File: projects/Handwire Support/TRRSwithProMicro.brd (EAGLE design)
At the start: 34.3 x 33 mm, 5 parts, among them SW1 RSTSWSMD

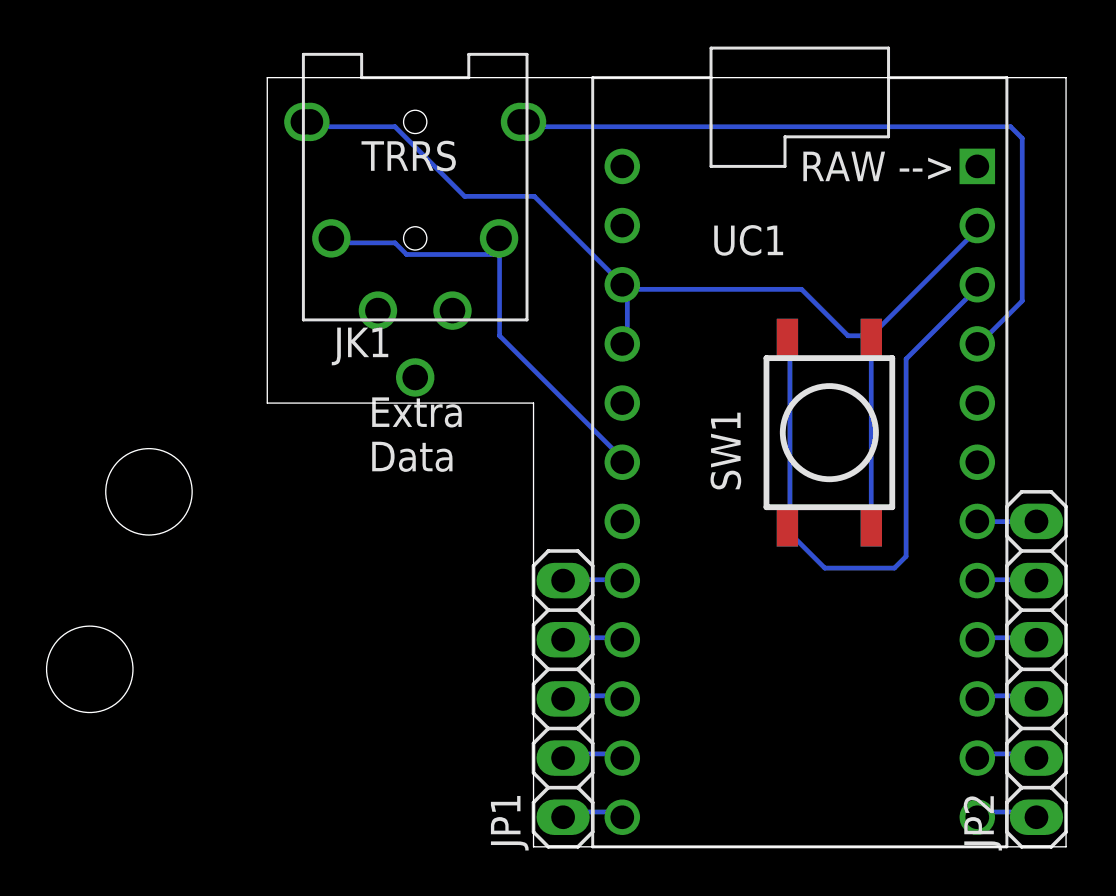
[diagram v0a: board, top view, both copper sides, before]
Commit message: Reversible handwires
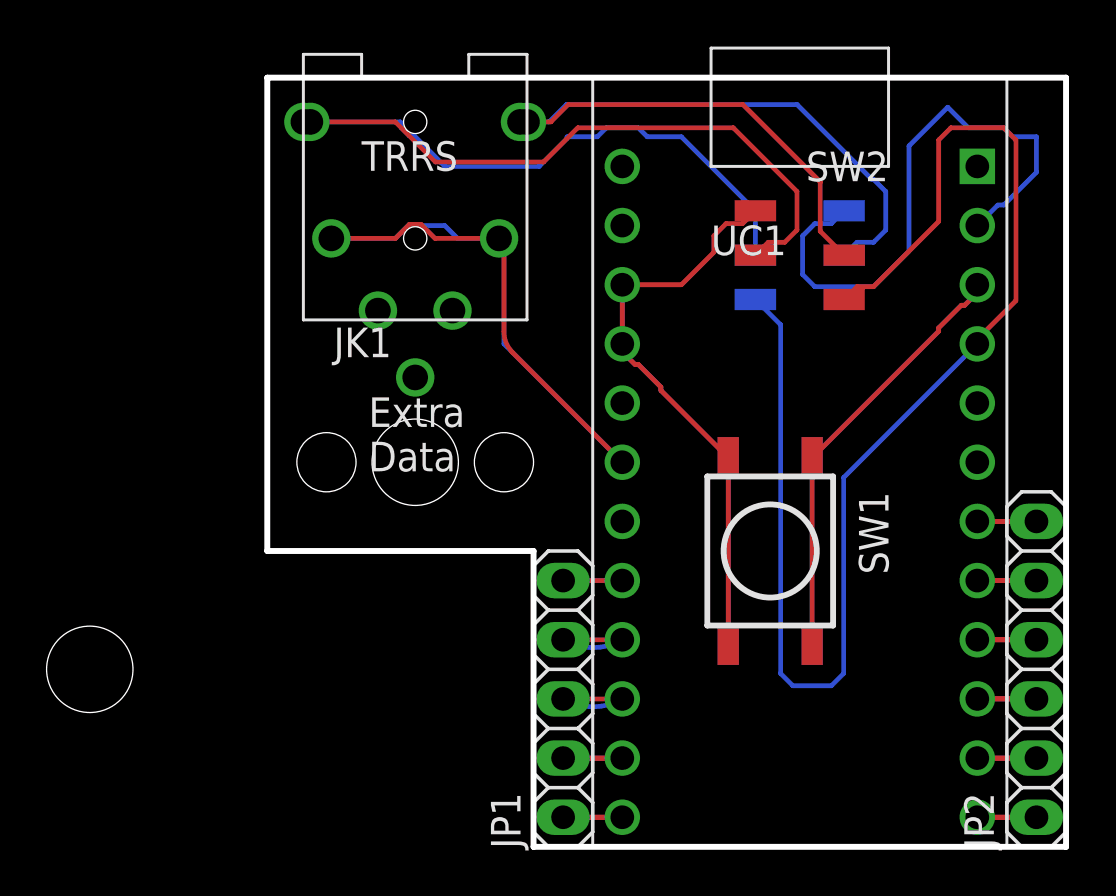
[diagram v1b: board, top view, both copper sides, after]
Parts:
- added SW2: TRANSFERPADDY, Keys:TRANSFER_PADS
- JK1: value TRRSJACK -> TRRSJACKOVER; device Keys:TRRSJACK -> Keys:TRRSJACK_OVER
- UC1: value PROMICROUNDER -> PROMICROTOP; device Keys:PROMICRO_UNDER -> Keys:PROMICRO
- moved SW1 5.68 mm to (21.6, 12.7), turned to 270 degrees
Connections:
- new net N$17: SW2.VCCB, SW2.VCCT, UC1.P$21
- new net N$4: JK1.4B, JK1.4T, SW2.IN4B, SW2.IN4T
- net N$1: now also SW2.IN1B, SW2.IN1T; no longer UC1.P$21
- net N$2: now also SW2.GNDB, SW2.GNDT; no longer JK1.4B, JK1.4T
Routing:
- net N$17: track 0.00 -> 58.3 mm
- net N$4: track 0.00 -> 51.7 mm
- net N$2: track 46.4 -> 68.1 mm
- net N$3: track 19.9 -> 38.9 mm
- net N$5: track 27.1 -> 36.9 mm
- net N$1: track 31.7 -> 39.0 mm
- net N$15: track 2.54 -> 7.62 mm
- net N$14: track 2.55 -> 7.62 mm
- net N$13: track 2.58 -> 7.62 mm
- net N$12: track 2.62 -> 7.62 mm
- net N$7: track 2.65 -> 7.62 mm
- net N$11: track 2.67 -> 7.62 mm
- net N$6: track 2.70 -> 7.62 mm
- net N$10: track 2.74 -> 7.62 mm
- net N$9: track 2.57 -> 6.12 mm
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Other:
- outline, holes or cut-outs redrawn
